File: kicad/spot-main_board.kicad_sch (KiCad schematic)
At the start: 20 parts, among them J1 Screw_Terminal_01x02, J2 Conn_01x04, J3 Screw_Terminal_01x02, J4 Screw_Terminal_01x08, Q1 BT139-600, Q2 Q_PMOS_DGS, U1 MOC3041M

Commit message: Restructure
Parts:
- added C? (x2): 22n, Capacitor_SMD:C_1206_3216Metric, symbol Device:C
- PS2: DigiKey PN (none) -> TMF05112-ND; MPN (none) -> TMF 05112; Manufacturer (none) -> Traco Power
- Q1: value BT139-600 -> BT139-600E/DG,127; DigiKey PN (none) -> 1740-1050-ND; MPN (none) -> BT139-600E/DG,127; Manufacturer (none) -> WeEn Semiconductors
- U1: value MOC3041M -> APT1232; footprint (none) -> Package_DIP:DIP-6_W7.62mm; DigiKey PN (none) -> 255-5968-ND
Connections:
- net +12V: now also C?.1, C?.1
- net GND: now also C?.2, C?.2
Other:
- note added: "Spot"
- note removed: "Spot 1"

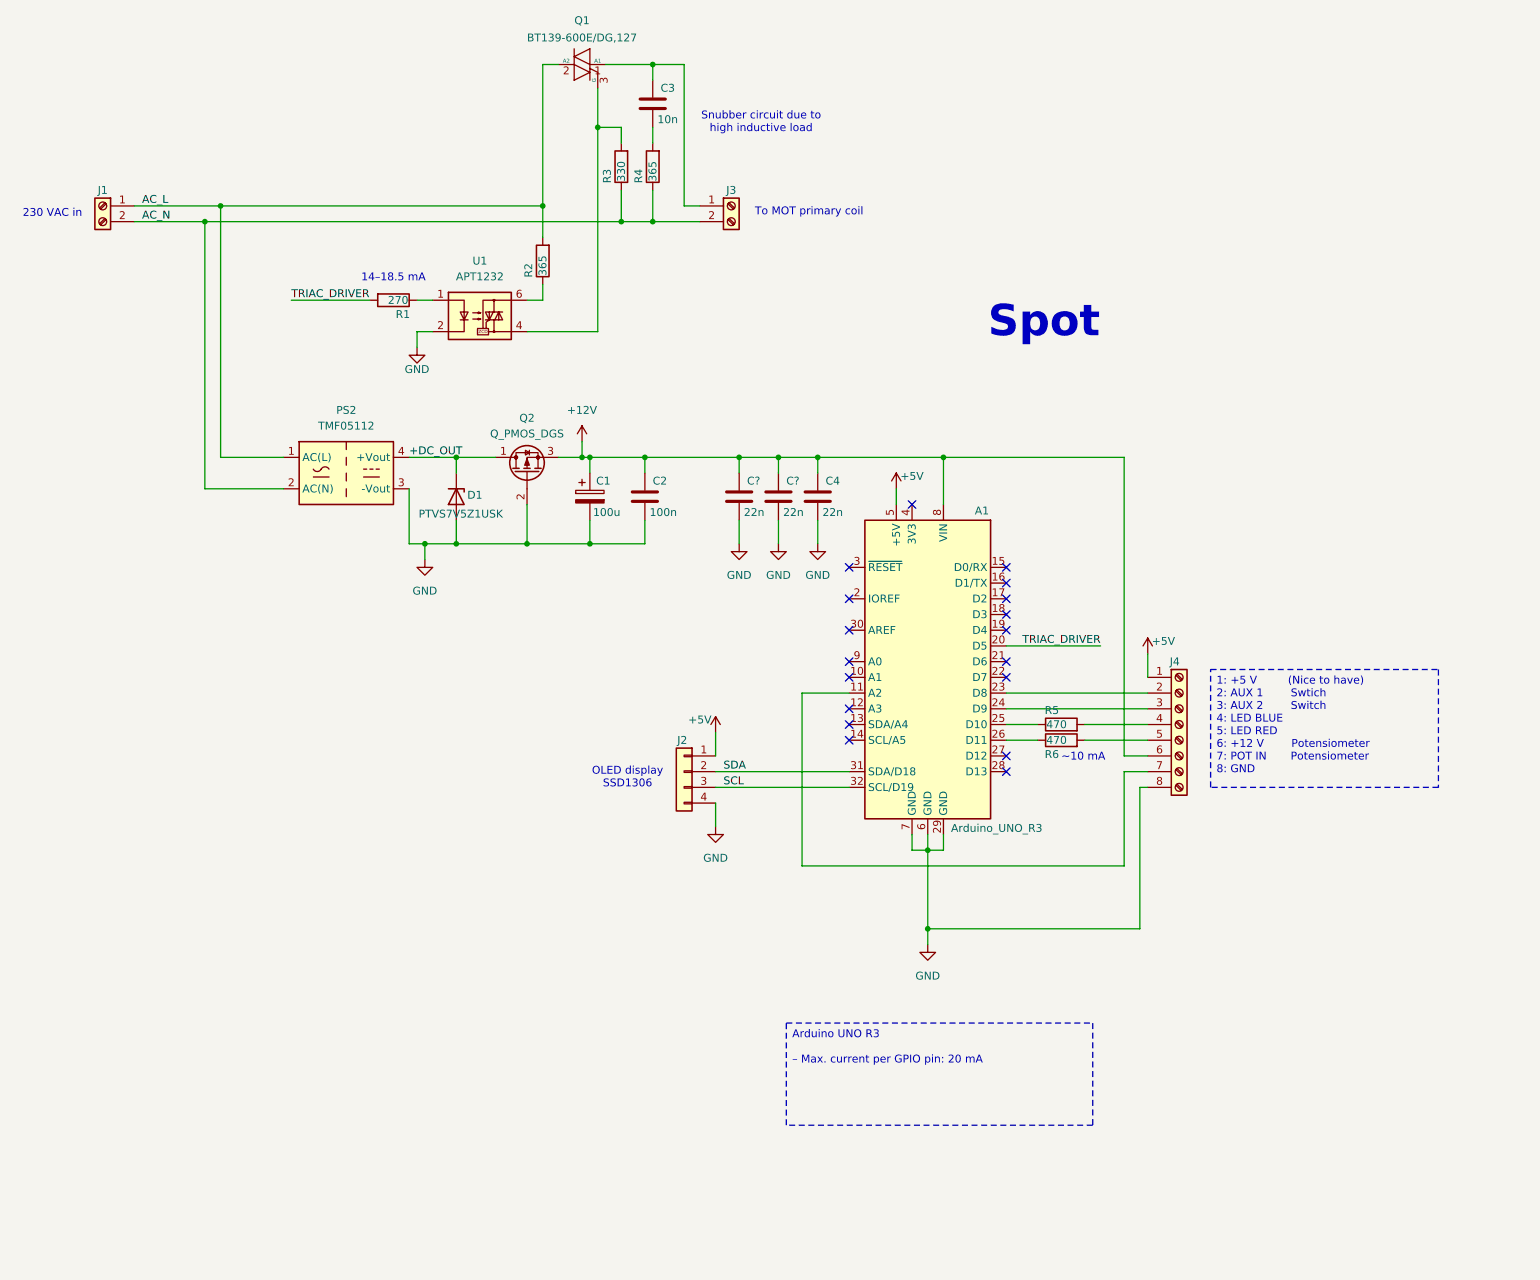
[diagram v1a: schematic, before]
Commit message: Add comments and cange to bidirectional TVS
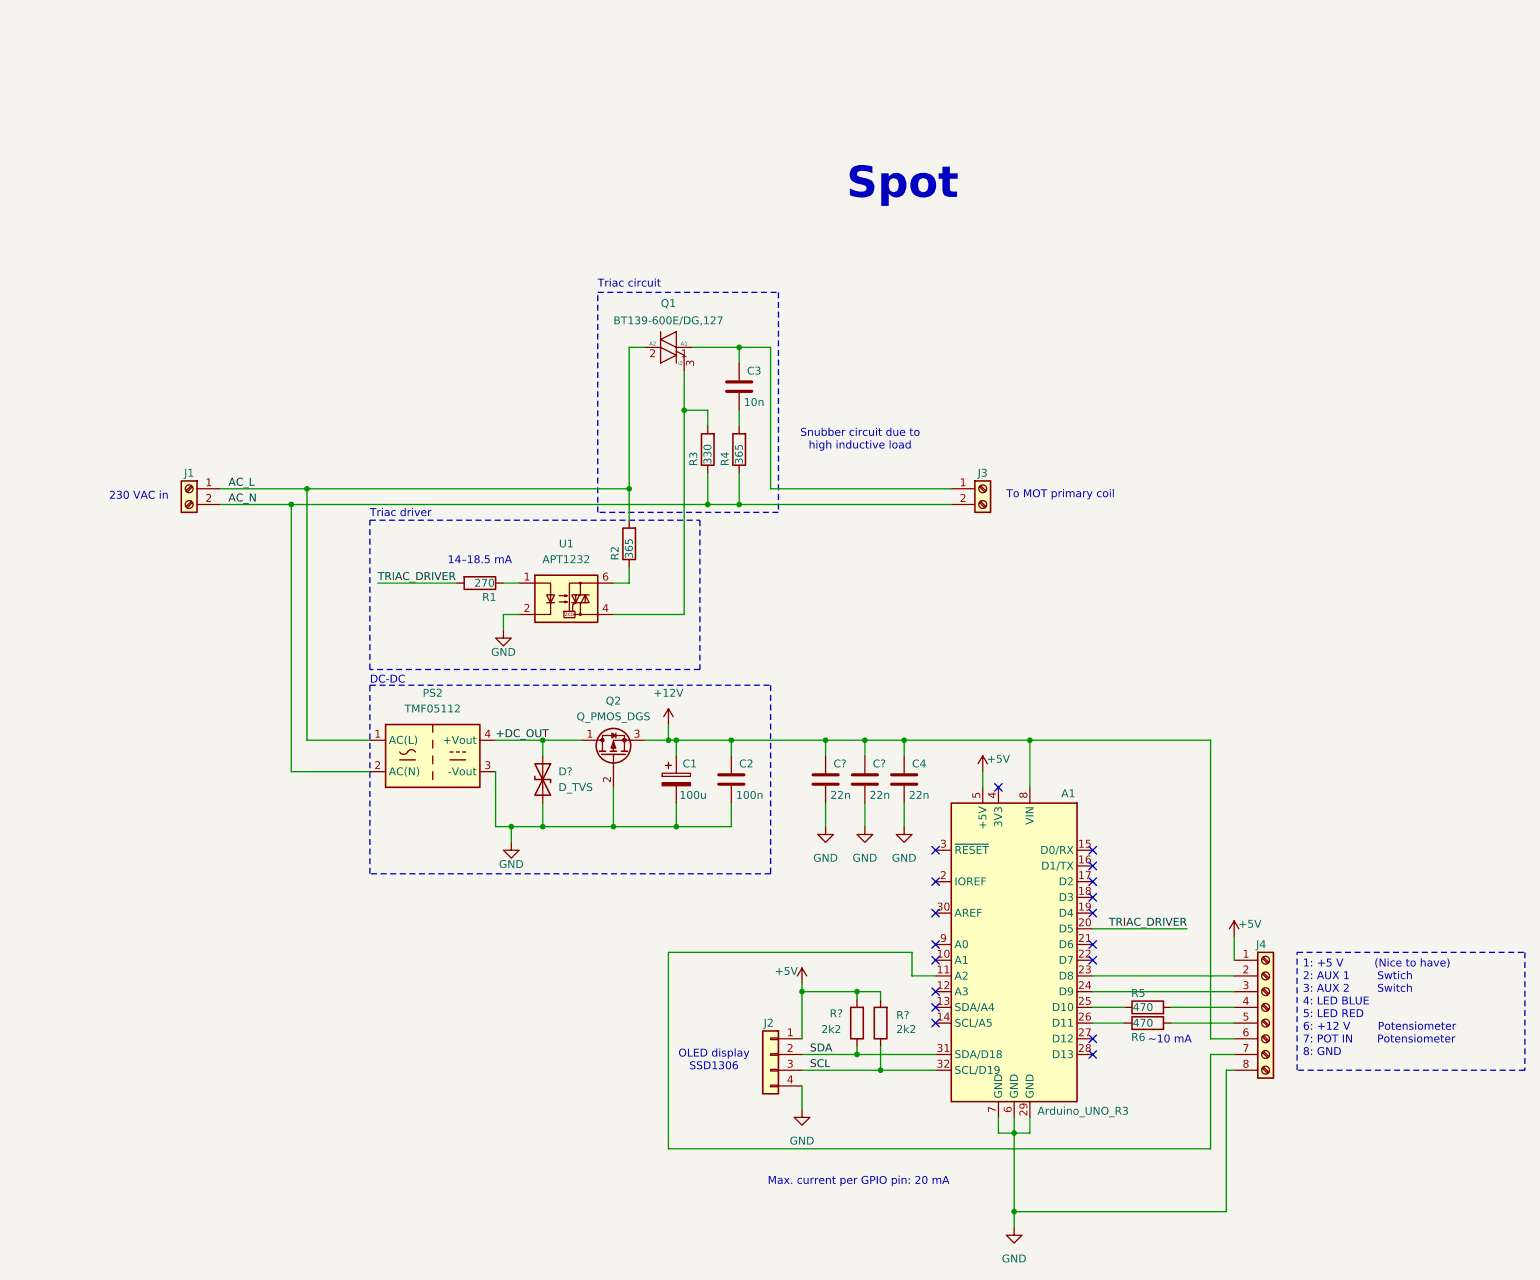
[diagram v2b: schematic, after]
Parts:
- removed D1: PTVS7V5Z1USK, Diode_SMD:Nexperia_DSN1608-2_1.6x0.8mm, symbol Diode:PTVS7V5Z1USK
- added D?: D_TVS, symbol Device:D_TVS
- added R? (x2): 2k2, Resistor_SMD:R_1206_3216Metric, symbol Device:R
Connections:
- net +5V: now also R?.2, R?.2
- net +DC_OUT: now also D?.1 (A1)
- net GND: now also D?.2 (A2)
- net SCL: now also R?.1
- net SDA: now also R?.1
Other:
- note added: "DC-DC"
- note added: "Max. current per GPIO pin: 20 mA"
- note added: "Triac circuit"
- note added: "Triac driver"
- moved on the sheet: A1, C1, C2, C3, C4, C?, J1, J2, J3, J4, PS2, Q1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
